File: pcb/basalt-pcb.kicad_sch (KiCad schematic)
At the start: 12 parts, among them J1 Conn_01x07_Pin, J2 Conn_01x07_Pin, J3 USB4215-03-A, J4 Conn_01x04_Pin, U1 DI78L3.3ZAB, U2 STM32C071F8Px

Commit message: Small pcb tweaks
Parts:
- J3: footprint footprints2:CONN_8p94X6p5X3p16_12L_GCC -> my-kicad-parts:USB4215-03-A
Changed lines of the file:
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@@
 			)
 		)
-		(property "Footprint" "footprints2:CONN_8p94X6p5X3p16_12L_GCC"
+		(property "Footprint" "my-kicad-parts:USB4215-03-A"
 			(at 77.47 80.01 0)
 			(hide yes)

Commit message: Minor edits to pcb and titleblocks
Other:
- company: (none) -> OC ECE MESA
- title: (none) -> MESA Basalt
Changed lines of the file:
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@@
 	(generator_version "10.0")
 	(paper "A4")
+	(title_block
+		(title "MESA Basalt")
+		(date "2026-05-02")
+		(rev "2")
+		(company "OC ECE MESA")
+	)
 	(junction
 		(at 85.09 82.55)

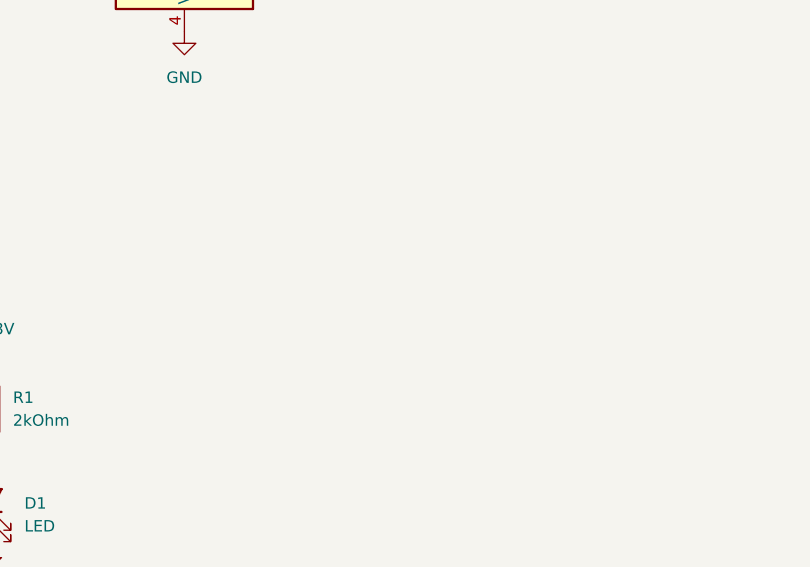
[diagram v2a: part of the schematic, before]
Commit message: Fix mounting holes
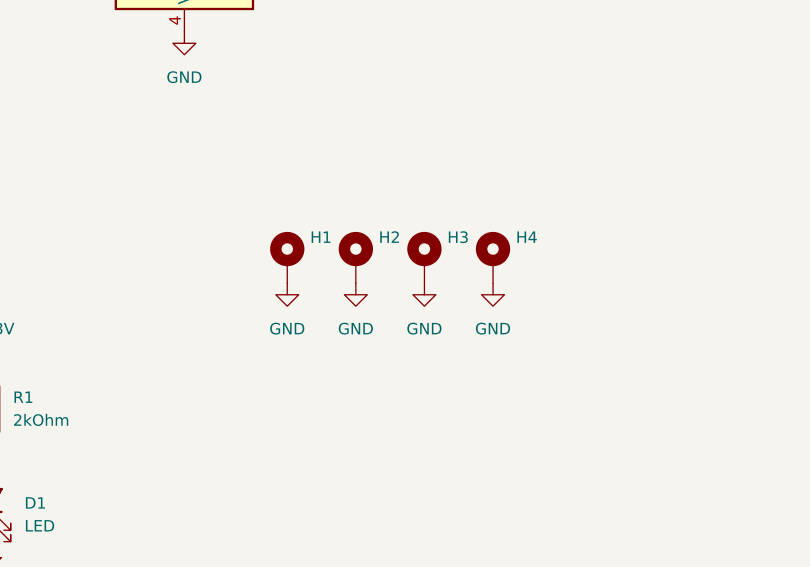
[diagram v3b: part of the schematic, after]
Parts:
- added H1, H2, H3, H4: MountingHole_Pad, MountingHole:MountingHole_2.2mm_M2_Pad, symbol Mechanical:MountingHole_Pad
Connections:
- net GND: now also H1.1, H2.1, H3.1, H4.1
